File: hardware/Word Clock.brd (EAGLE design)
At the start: 33 x 33 mm, 27 parts, among them IC1 DS3231/SO, Q1 MMBT2222A, U1 ATMEGA328P-AU

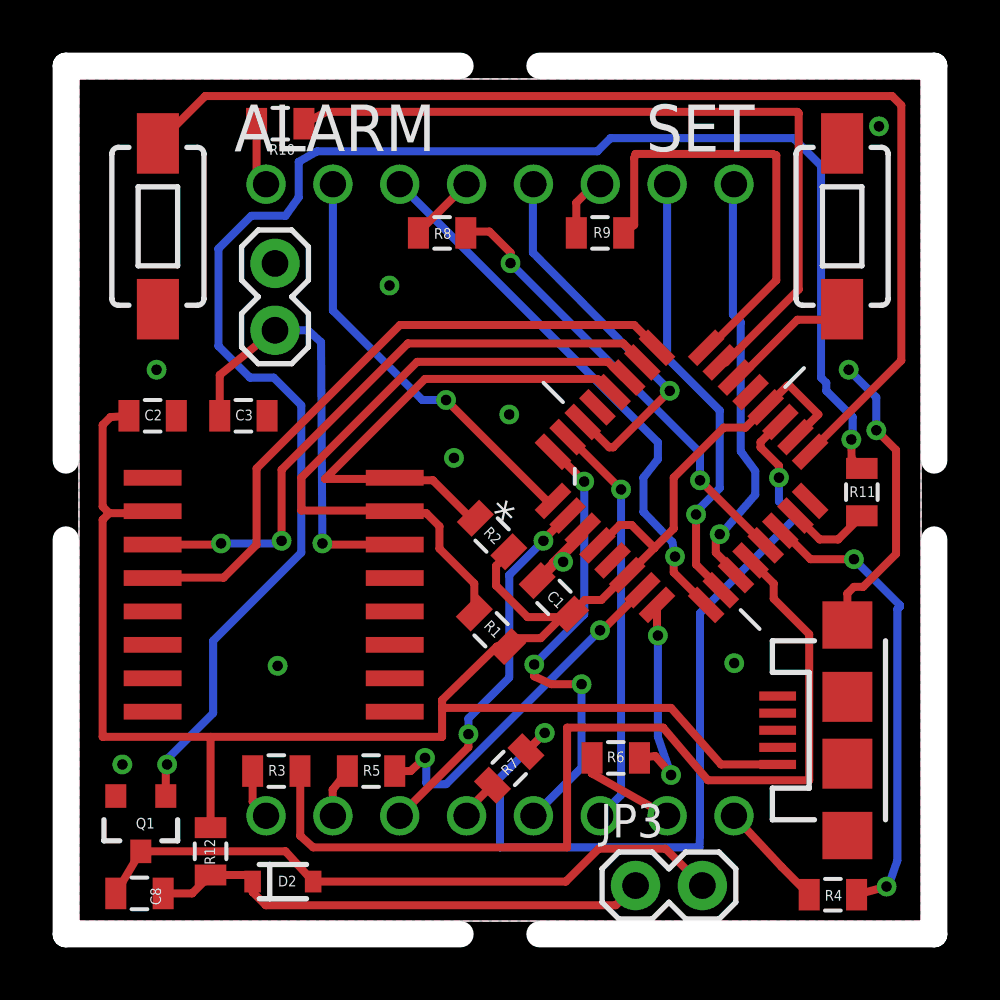
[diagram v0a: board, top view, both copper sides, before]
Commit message: Fixing errant use of ADC lines and revised for 0.6mm vias.
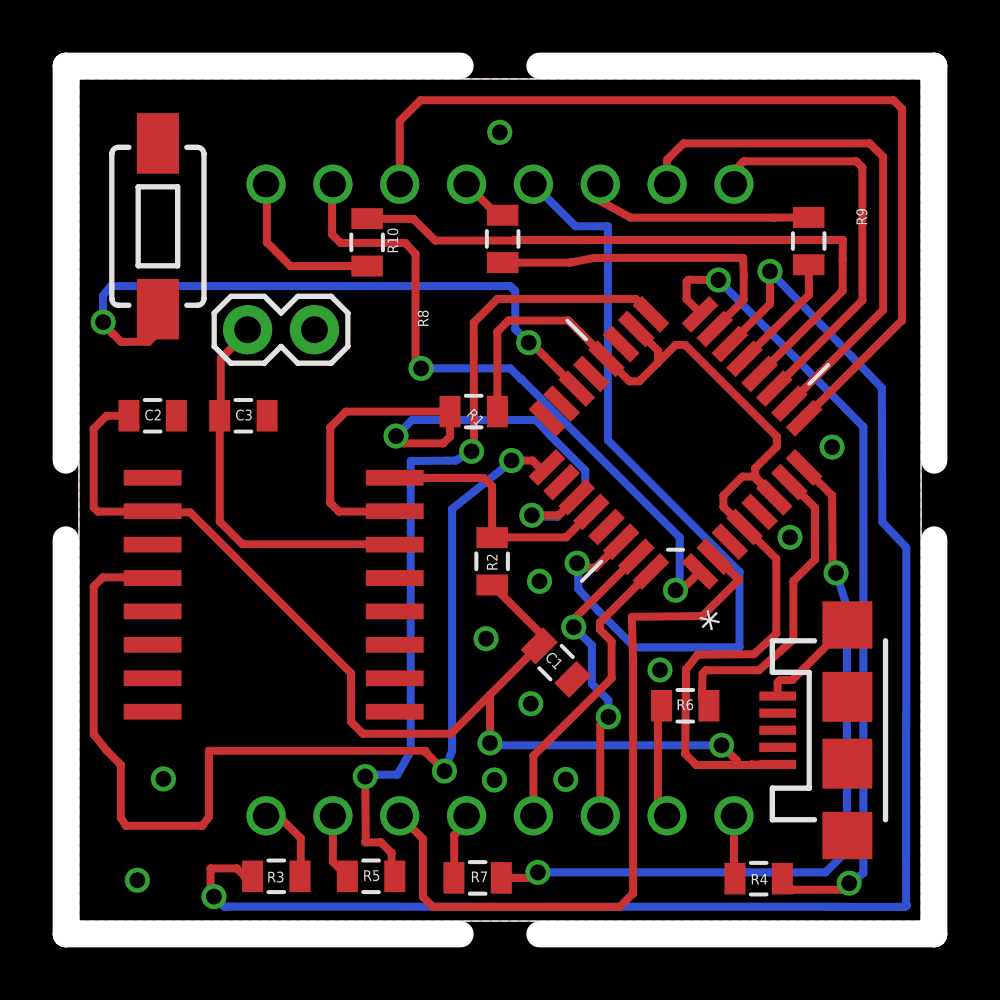
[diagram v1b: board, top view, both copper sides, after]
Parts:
- removed C8: 0.1uF, SparkFun-Capacitors:0805
- removed D2: 1N4001, SparkFun-DiscreteSemi:SOD-323
- removed JP3: M02PTH, SparkFun-Connectors:1X02
- removed Q1: MMBT2222A, SparkFun-DiscreteSemi:SOT23-3
- removed R11: 1k, SparkFun-Resistors:0805
- removed R12: 33, SparkFun-Resistors:0805
- removed S2: SWITCH-MOMENTARY-2SMD-1101NE, SparkFun-Electromechanical:TACTILE-SWITCH-1101NE
- moved S1 26.0 mm to (3.00, 26.4)
- moved R1 8.32 mm to (15.0, 19.4), turned to 0 degrees
- moved R9 7.94 mm to (27.7, 25.8), turned to 90 degrees
- moved R10 5.59 mm to (10.9, 25.8), turned to 270 degrees
- moved R7 4.33 mm to (15.2, 1.64), turned to 0 degrees
- moved R3 4.00 mm to (7.50, 1.70), turned to 180 degrees
- moved R5 4.00 mm to (11.1, 1.70)
- moved R6 3.30 mm to (23.0, 8.18)
- moved R4 2.89 mm to (25.8, 1.61)
- moved C1 2.48 mm to (18.1, 9.82), turned to 315 degrees
- moved R8 2.31 mm to (16.1, 25.9), turned to 270 degrees
- moved U1 1.29 mm to (22.7, 18.2), turned to 135 degrees
- moved JP2 1.04 mm to (6.41, 22.5), turned to 0 degrees
- moved R2 1.00 mm to (15.7, 13.7), turned to 270 degrees
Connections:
- removed net INT: IC1.3, U1.26
- removed net MISO: U1.16
- removed net MOSI: R11.2, U1.15
- removed net N$16: R7.2, U1.19
- removed net N$27: Q1.1, R11.1
- removed net N$28: C8.1, D2.C, JP3.1, R12.1
- removed net N$29: C8.2, D2.A, JP3.2, Q1.3
- removed net SCK: S2.1, U1.17
- new net N$30: R6.2, U1.7
- new net N$31: R7.2, U1.8
- new net N$33: R3.2, U1.14
- net 5V: no longer R12.2
- net GND: no longer Q1.2, S2.2
- net N$10: no longer R10.1
- net N$11: now also R9.1, U1.13; no longer R3.2, U1.12
- net N$12: now also U1.15; no longer U1.13
- net N$13: now also U1.16; no longer U1.14
- net N$14: now also U1.17; no longer U1.7
- net N$15: now also R10.1, U1.12; no longer R6.2, U1.8
- net N$9: no longer R9.1
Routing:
- net N$27: track 62.8 -> 0.00 mm, vias 2 -> 0
- net N$33: track 0.00 -> 59.0 mm, vias 0 -> 2
- net SCK: track 43.7 -> 0.00 mm
- net N$16: track 32.7 -> 0.00 mm, vias 2 -> 0
- net N$11: track 36.7 -> 4.59 mm
- net N$10: track 29.7 -> 0.00 mm
- net N$31: track 0.00 -> 28.8 mm, vias 0 -> 2
- net N$29: track 24.8 -> 0.00 mm
- net INT: track 23.7 -> 0.00 mm, vias 2 -> 0
- net N$28: track 19.3 -> 0.00 mm
- net N$18: track 5.87 -> 25.1 mm, vias 0 -> 2
- net N$14: track 13.9 -> 32.6 mm
- net N$1: track 14.6 -> 31.8 mm
- net N$9: track 17.0 -> 0.00 mm
- net N$15: track 8.11 -> 24.8 mm, vias 2 -> 0
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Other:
- board text removed: "ALARM"
- board text removed: "SET"

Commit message: 0.7mm for rivets.
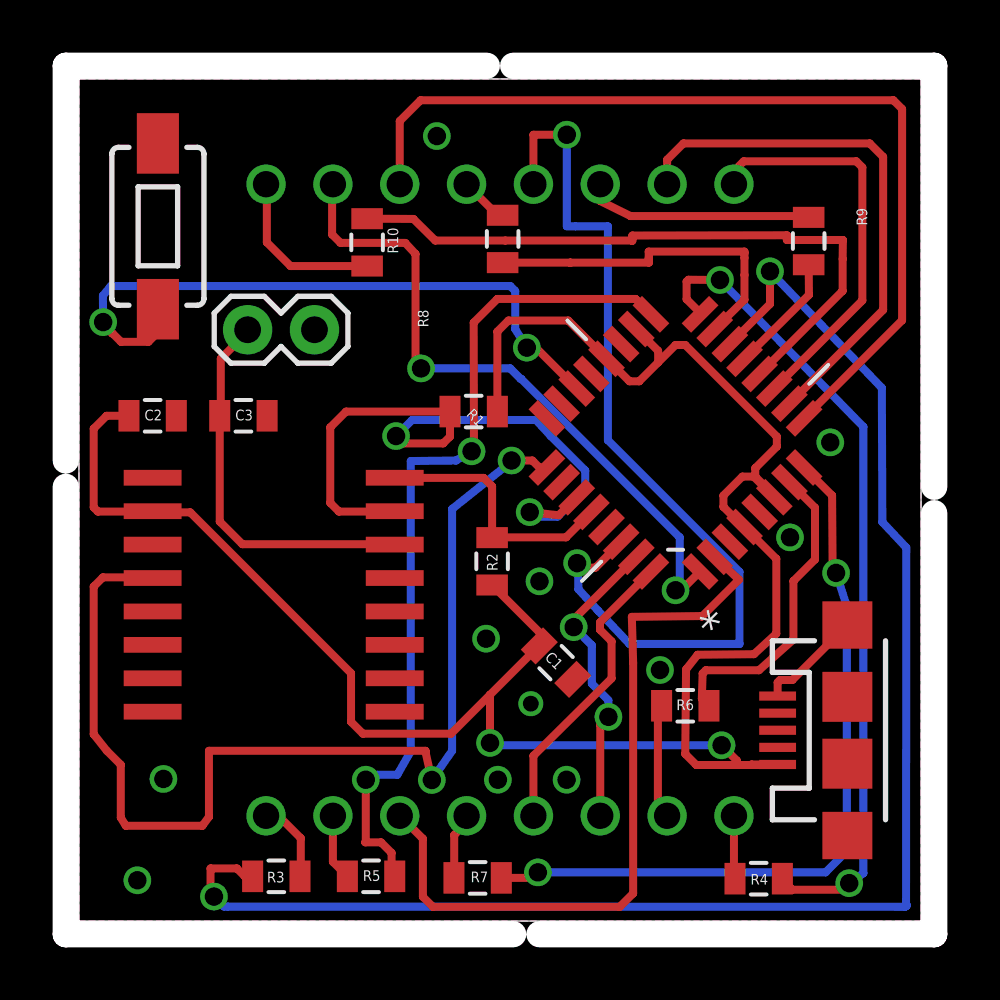
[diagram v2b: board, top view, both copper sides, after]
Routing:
- net N$1: track 31.8 -> 36.3 mm, vias 1 -> 2
- net RST: track 41.7 -> 42.4 mm
- net N$12: track 12.3 -> 13.0 mm
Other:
- outline, holes or cut-outs redrawn
